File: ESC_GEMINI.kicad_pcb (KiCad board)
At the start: 6 copper layers, 12 x 35 mm, 97 parts, among them P1 V, P10 Solder Pad, P11 Solder Pad, P2 G, P3 TX, P4 RX, P5 D, P6 K, P7 Solder Pad, P8 Solder Pad, P9 Solder Pad, Q1 HSBA4052, Q2 HSBA4052, Q3 HSBA4052, Q4 HSBA4052, Q5 HSBA4052, Q6 HSBA4052, U1 AT32F413KCU7-4, U2 GM7333, U3 LGS5148, U4 DRV8300D, U5 INA199A1, U6 INA199A1

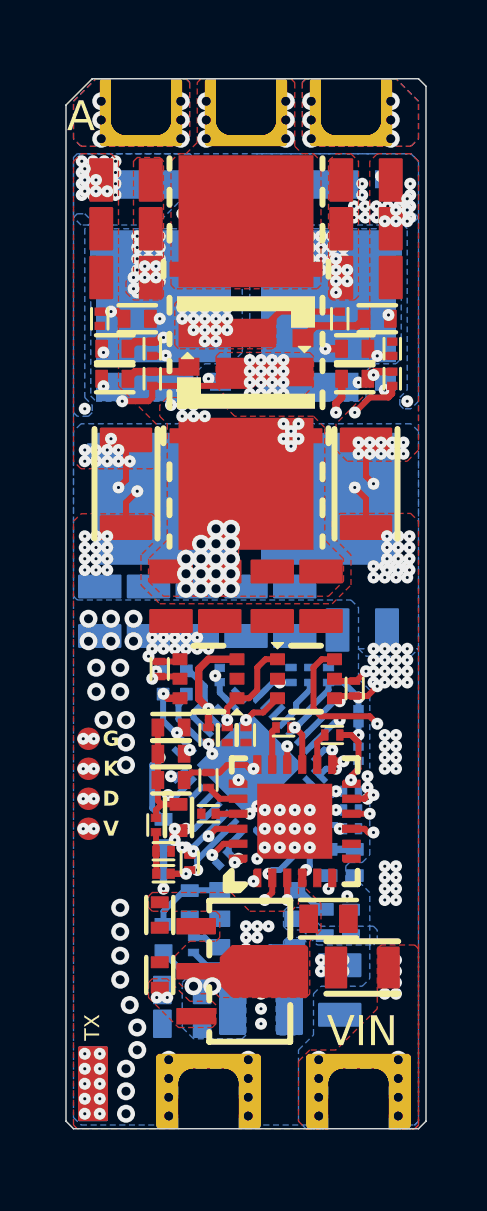
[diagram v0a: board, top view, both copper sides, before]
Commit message: Update layout and modified sense amplifier
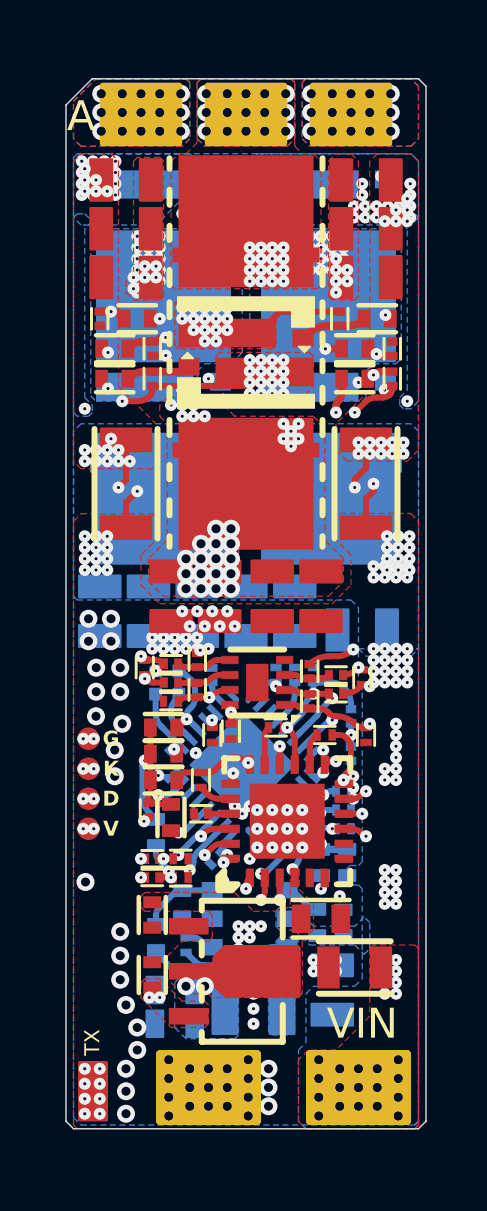
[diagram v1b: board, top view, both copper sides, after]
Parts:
- removed C27, C29: 10nF, 001_GN_RCL_SMD:C0201(0603M)
- removed C47: 100nF, 001_GN_RCL_SMD:C0201(0603M)
- removed U5, U6: INA199A1, 003_GN_SMALL-SEMI_SMD:SOT-363
- added C1: 100pF, 001_GN_RCL_SMD:C0201(0603M), F.Cu at (97.8, 104.1)
- added C15: 100pF, 001_GN_RCL_SMD:C0201(0603M), F.Cu at (97.5, 98.2)
- added C5: 100pF, 001_GN_RCL_SMD:C0201(0603M), F.Cu at (97.8, 103.5)
- added C6: 100pF, 001_GN_RCL_SMD:C0201(0603M), F.Cu at (104.0, 99.4)
- added R32: 510R, 001_GN_RCL_SMD:R0201(0603M), F.Cu at (96.9, 103.5)
- added R33: 510R, 001_GN_RCL_SMD:R0201(0603M), F.Cu at (96.9, 104.1)
- added R34: 10k, 001_GN_RCL_SMD:R0201(0603M), F.Cu at (97.5, 97.6)
- added R35: 1Meg, 001_GN_RCL_SMD:R0201(0603M), F.Cu at (98.4, 97.9)
- added R36: 1Meg, 001_GN_RCL_SMD:R0201(0603M), F.Cu at (98.4, 96.9)
- added R37: 10k, 001_GN_RCL_SMD:R0201(0603M), F.Cu at (103.0, 97.4)
- added R38: 10k, 001_GN_RCL_SMD:R0201(0603M), F.Cu at (103.0, 98.0)
- added R39: 1Meg, 001_GN_RCL_SMD:R0201(0603M), F.Cu at (102.1, 97.2)
- added R40: 1Meg, 001_GN_RCL_SMD:R0201(0603M), F.Cu at (102.1, 98.2)
- added U7: GS8052, 003_GN_SMALL-SEMI_SMD:DFN-8_2020, F.Cu at (100.4, 97.6)
- Q1, Q2, Q3, Q4, Q5, Q6: value HSBA4052 -> APG024N04G
- R11: value 68k -> 100k
- R17, R18, R19, R20, R23, R24: value 2.2R -> 5.1R
- R6: value 100 -> 100R
- R8: value 100 -> 10k
- U4: value DRV8300D -> DRV8300DRGER
- moved R8 7.00 mm to (97.5, 97.0)
- moved R6 0.56 mm to (96.8, 101.9)
- moved C45 0.52 mm to (99.5, 99.2)
- moved C49 0.50 mm to (96.6, 97.1)
- moved C18 0.50 mm to (101.6, 97.4)
- moved C20 0.50 mm to (101.0, 97.4)
- moved C22 0.50 mm to (102.2, 97.4)
- moved C46 0.50 mm to (98.9, 99.4)
- moved C48 0.45 mm to (103.9, 97.5), turned to -90 degrees
- moved C17 0.25 mm to (103.2, 101.9)
- moved C19 0.25 mm to (103.2, 101.2)
- moved C21 0.25 mm to (99.0, 103.5)
- moved C24 0.25 mm to (102.9, 107.9)
- moved C25 0.25 mm to (96.9, 105.4)
- moved C26 0.25 mm to (103.2, 105.6)
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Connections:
- P3 pad PAD: /CTRL/PWM_IN-P -> Net-(P3-PadPAD)
- P4 pad PAD: /CTRL/PWM_IN-N -> Net-(P4-PadPAD)
- R6 pad 2: Net-(C27-Pad1) -> /CTRL/BEMF_U
- R8 pad 1: Net-(C27-Pad1) -> /GND_A
- R8 pad 2: /CTRL/BEMF_U -> Net-(U7B-IN_B+)
- U1 pad 7: /CTRL/I_SNS_B -> /CTRL/I_SNS_C
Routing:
- net +3V3: track 38.7 -> 29.4 mm, vias 13 -> 12
- net /CTRL/I_SNS_B: track 7.92 -> 0.00 mm, vias 3 -> 0
- net Net-(P3-PadPAD): track 0.00 -> 7.87 mm, vias 0 -> 11
- net Net-(P4-PadPAD): track 0.00 -> 7.54 mm, vias 0 -> 11
- net /CTRL/PWM_IN-P: track 16.5 -> 9.08 mm, vias 13 -> 3
- net /CTRL/PWM_IN-N: track 16.2 -> 8.85 mm, vias 13 -> 3
- net /CTRL/I_SNS_C: track 0.00 -> 6.39 mm, vias 0 -> 3
- net /CTRL/VREF_U: track 14.4 -> 20.6 mm, vias 4 -> 8
- net Net-(U7B-IN_B+): track 0.00 -> 1.81 mm
- net /CTRL/BEMF_U: track 10.6 -> 8.77 mm
- net Net-(U7B-IN_B-): track 0.00 -> 1.79 mm
- net Net-(U7A-IN_A+): track 0.00 -> 1.53 mm
- net Net-(U7A-IN_A-): track 0.00 -> 1.48 mm
- net /CTRL/PHC: track 27.1 -> 25.6 mm, vias 39 -> 47
- net Net-(C27-Pad1): track 1.39 -> 0.00 mm
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- added copper zone on In4.Cu, net +3V3
- added copper zone on B.Cu, net /CTRL/PHB
- added copper zone on In1.Cu, net Net-(P3-PadPAD)
- added copper zone on In4.Cu, net Net-(P4-PadPAD)
- removed copper zone on In4.Cu, net /CTRL/PWM_IN-N
- removed copper zone on In1.Cu, net /CTRL/PWM_IN-P
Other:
- board text added: "GND"
- board text added: "v1.1(230915)"
- board text added: "邮票孔"
- board text removed: "v1.0(230823)"

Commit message: Modified the scheme of current sensing
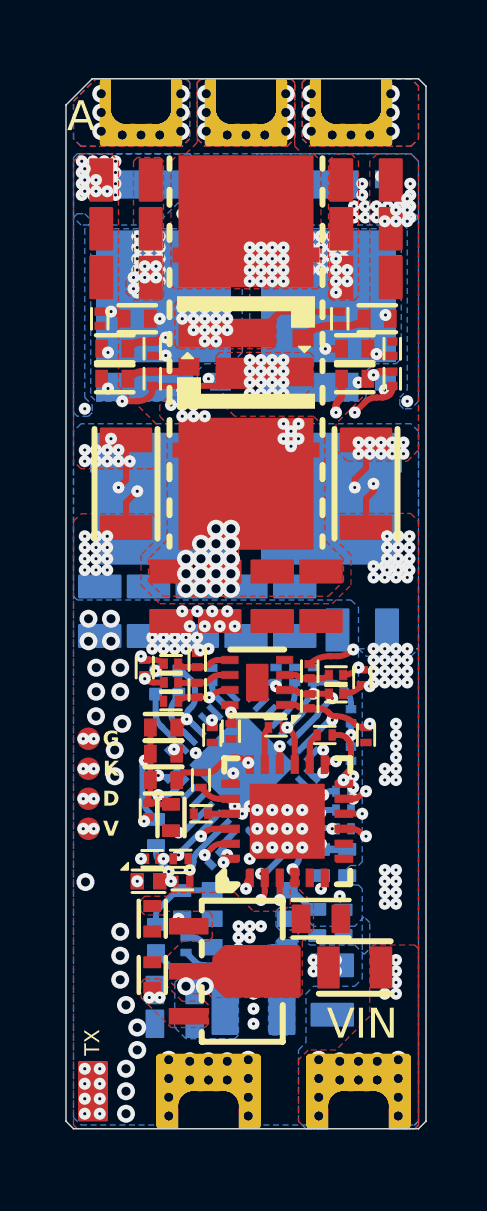
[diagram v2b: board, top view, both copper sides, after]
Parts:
- removed R33: 510R, 001_GN_RCL_SMD:R0201(0603M)
- added D2: DS520-30EAA02, 002_GN_TWO-PIN_PLASTIC_SMD:DFN-2_1006, F.Cu at (96.8, 104.2)
- added REF**: Tab, PCM_kikit:Tab, F.Cu at (106.2, 90.6)
- added REF**: Tab, PCM_kikit:Tab, F.Cu at (93.8, 90.6)
- added REF**: Tab, PCM_kikit:Tab, F.Cu at (106.2, 104.4)
- added REF**: Tab, PCM_kikit:Tab, F.Cu at (100.0, 112.8)
- added REF**: Tab, PCM_kikit:Tab, F.Cu at (100.0, 77.2)
- added REF**: Tab, PCM_kikit:Tab, F.Cu at (93.8, 104.4)
- C24: value 4.7uF -> 10uF
- R16: value 100k -> NC/100k
- R34, R37, R38, R8: value 10k -> 1k
- R35, R36, R39, R40: value 1Meg -> 100k
- R6: value 100R -> 0R
- moved C1 0.13 mm to (97.9, 104.2)
- moved C25 0.12 mm to (96.9, 105.5)
- moved P10 0.12 mm to (100.0, 77.5)
- moved P11 0.12 mm to (103.5, 77.5)
- moved P7 0.12 mm to (103.8, 112.5)
- moved P8 0.12 mm to (98.8, 112.5)
- moved P9 0.12 mm to (96.5, 77.5)
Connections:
- net +6V renamed +8V
- U1 pad 32: unconnected-(U1C-PB8-Pad32) -> GND
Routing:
- net VBUS: vias 123 -> 121
- net GND: vias 178 -> 174
- net /CTRL/PHC: vias 47 -> 42
- net /CTRL/PHB: vias 63 -> 58
- net /CTRL/PHA: vias 46 -> 41
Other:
- board text added: "v1.2(231013)"
- board text removed: "GND"
- board text removed: "v1.1(230915)"
